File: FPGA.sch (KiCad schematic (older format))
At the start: 9 parts, among them U34 PCA9555AHF, U39 PCA9555AHF

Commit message: SCH: connect SI570_OE to U39 P0_0 (pin 1)
... also rotated 6 net labels to make the
little _not connected_ square disappear
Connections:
- net labels added: SI570_OE
- wire segments 147 -> 148
- no-connect marks 4 -> 3
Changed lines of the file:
@@
 I2C_APP_SDA
 NoConn ~ 8500 8950
-NoConn ~ 8500 9050
 NoConn ~ 8500 9850
 NoConn ~ 8500 9950
@@
 	1    0    0    -1
 $EndComp
+Text HLabel 8950 9050 2    50   Output ~ 10
+SI570_OE
+Wire Wire Line
+	8500 9050 8950 9050
 $EndSCHEMATC

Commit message: Start adding isolation for I2C_FPGA_SW_RST and EXP_INT
Adds U47, another TCA9517
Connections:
- net labels removed: +3V3
- wire segments 148 -> 149
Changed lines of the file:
@@
 Wire Wire Line
 	8550 3550 8700 3550
-$Comp
-L power:+3V3 #PWR?
-U 1 1 5DA3DD5C
-P 1100 8400
-AR Path="/5BD32060/5DA3DD5C" Ref="#PWR?"  Part="1"
-AR Path="/5C907554/5C417BCB/5DA3DD5C" Ref="#PWR?"  Part="1"
-AR Path="/5C907554/5DA3DD5C" Ref="#PWR0548"  Part="1"
-AR Path="/5C907554/5CAAC367/5DA3DD5C" Ref="#PWR?"  Part="1"
-F 0 "#PWR0548" H 1100 8250 50  0001 C CNN
-F 1 "+3V3" H 1115 8573 50  0000 C CNN
-F 2 "" H 1100 8400 50  0001 C CNN
-F 3 "" H 1100 8400 50  0001 C CNN
-	1    1100 8400
-	1    0    0    -1
-$EndComp
 Wire Wire Line
 	1100 9050 1100 8700
@@
 Wire Wire Line
 	8500 9050 8950 9050
+$Comp
+L power:+3V3P #PWR?
+U 1 1 5F5802EE
+P 1100 8350
+AR Path="/5C16C03C/5F5802EE" Ref="#PWR?"  Part="1"
+AR Path="/5BCEDA39/5F5802EE" Ref="#PWR?"  Part="1"
+AR Path="/5D05A99E/5F5802EE" Ref="#PWR?"  Part="1"
+AR Path="/5C16BF8E/5F5802EE" Ref="#PWR?"  Part="1"
+AR Path="/5CA40231/5F5802EE" Ref="#PWR?"  Part="1"
+AR Path="/5F5802EE" Ref="#PWR?"  Part="1"
+AR Path="/5BCEDA3D/5F5802EE" Ref="#PWR?"  Part="1"
+AR Path="/5C907554/5F5802EE" Ref="#PWR0548"  Part="1"
+F 0 "#PWR0548" H 1100 8200 50  0001 C CNN
+F 1 "+3V3P" H 1115 8523 50  0000 C CNN
+F 2 "" H 1100 8350 50  0001 C CNN
+F 3 "" H 1100 8350 50  0001 C CNN
+	1    1100 8350
+	1    0    0    -1
+$EndComp
+Wire Wire Line
+	1100 8400 1100 8350
 $EndSCHEMATC

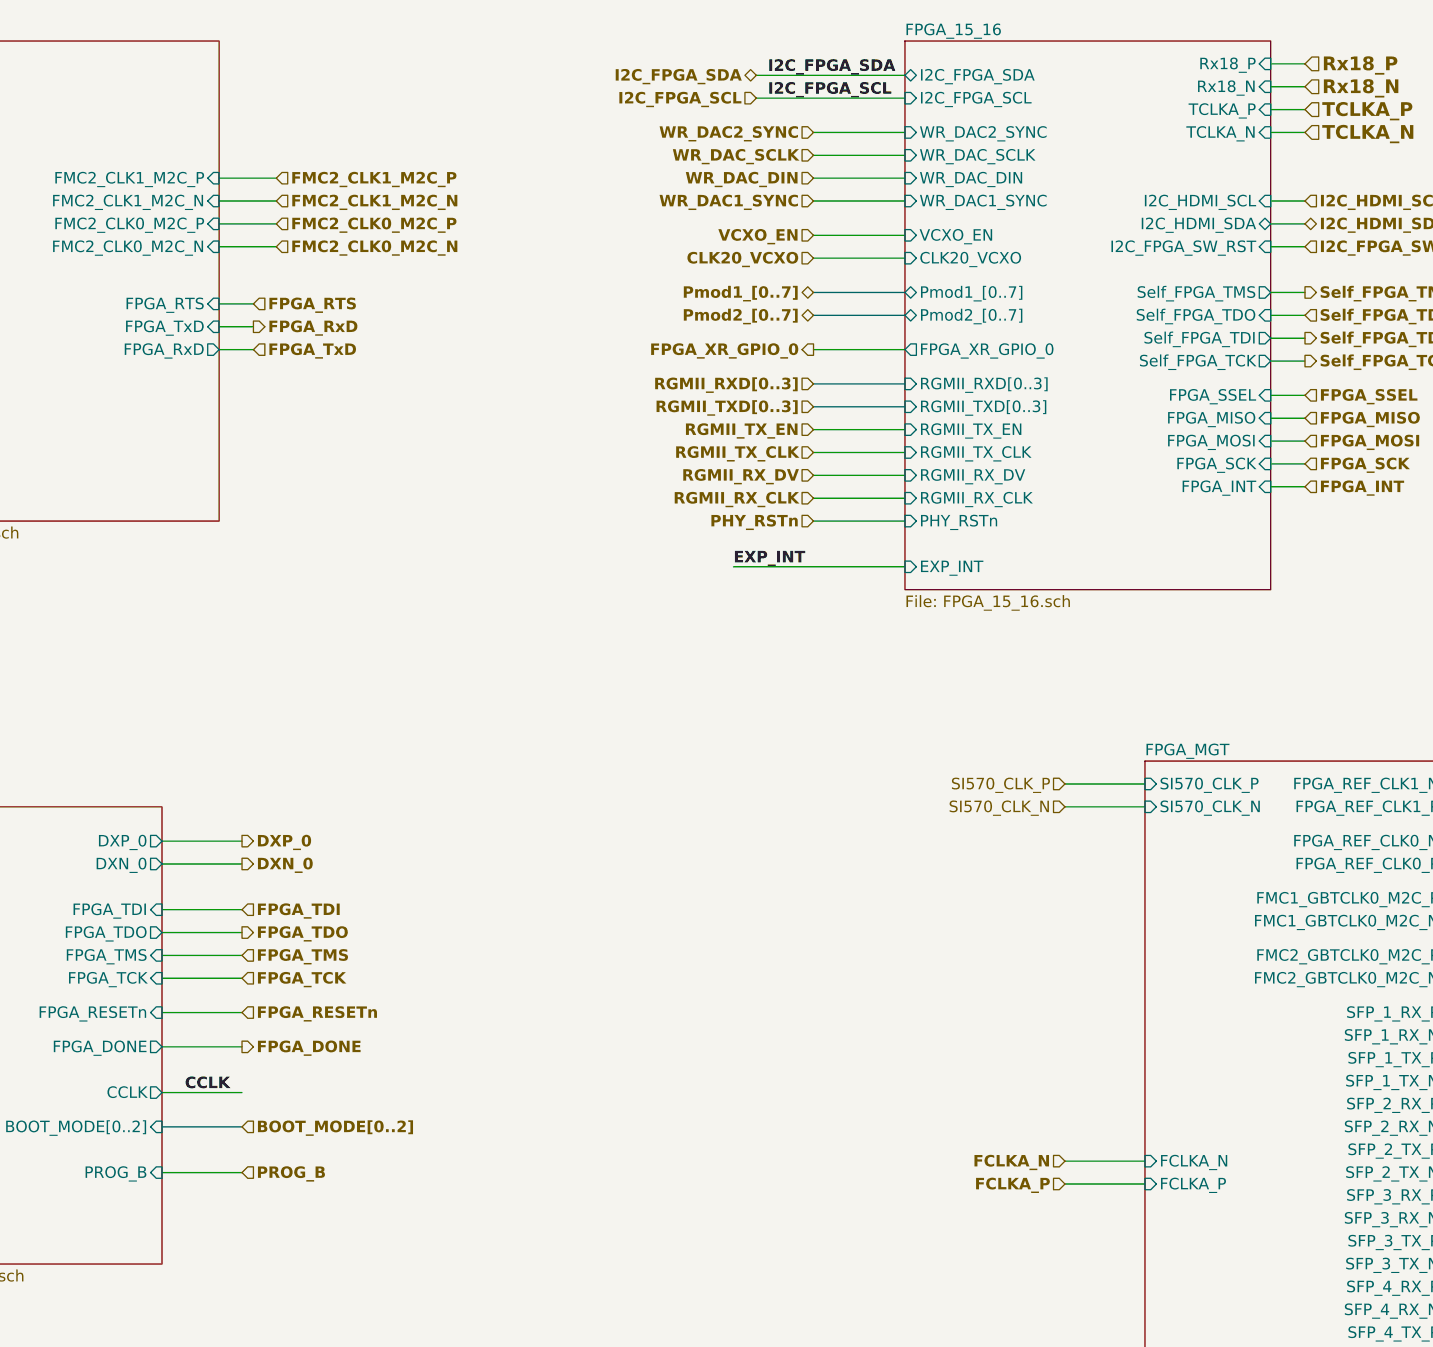
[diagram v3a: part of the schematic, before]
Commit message: sch: connect FPGA_DONE to U46, U47
also clean up some overlapping elements
and miss-aligned labels
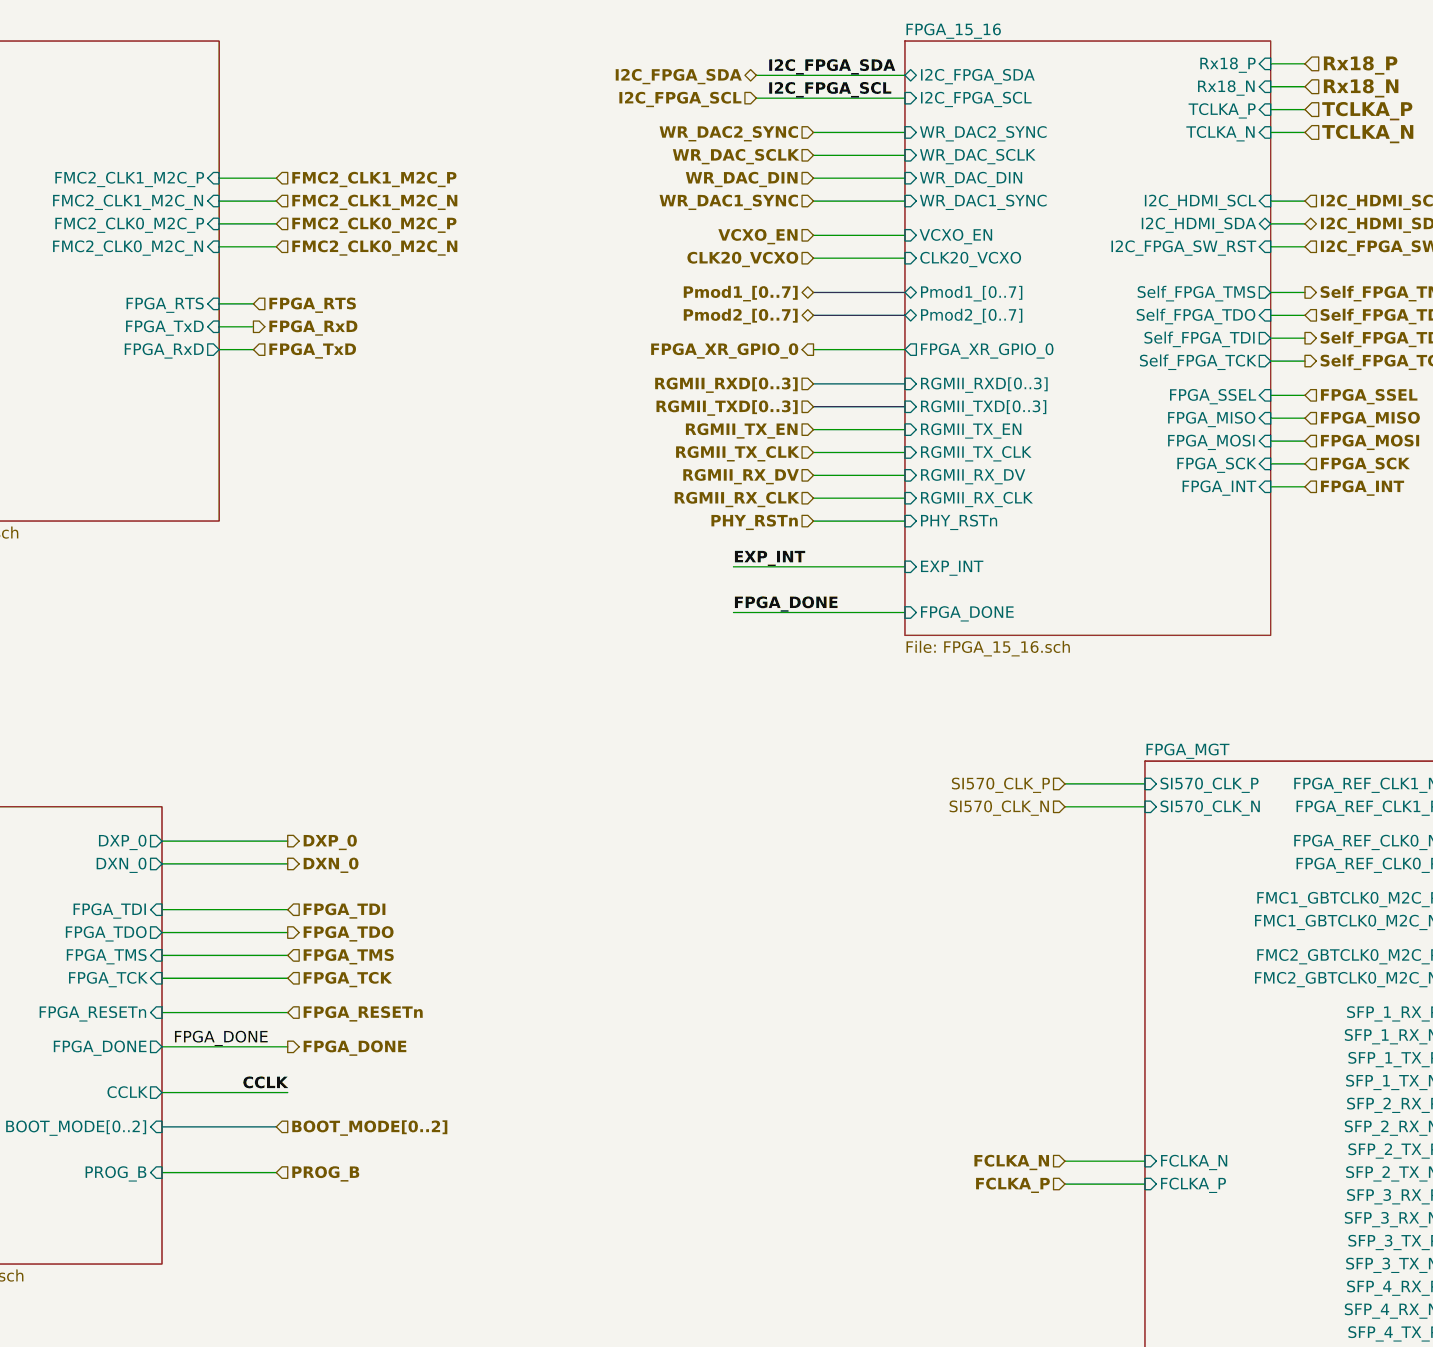
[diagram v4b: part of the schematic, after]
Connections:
- wire segments 149 -> 150
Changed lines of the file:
@@
 Comment4 ""
 $EndDescr
-Text HLabel 4050 5950 2    50   Input ~ 10
+Text HLabel 4250 5950 2    50   Input ~ 10
 FPGA_RESETn
 $Sheet
@@
 F12 "PROG_B" I R 3700 6650 50
 $EndSheet
-Wire Wire Line
-	3700 5950 4050 5950
-Text HLabel 4050 5500 2    50   Input ~ 10
+Text HLabel 4250 5500 2    50   Input ~ 10
 FPGA_TDI
-Text HLabel 4050 5600 2    50   Output ~ 10
+Text HLabel 4250 5600 2    50   Output ~ 10
 FPGA_TDO
-Text HLabel 4050 5700 2    50   Input ~ 10
+Text HLabel 4250 5700 2    50   Input ~ 10
 FPGA_TMS
-Text HLabel 4050 5800 2    50   Input ~ 10
+Text HLabel 4250 5800 2    50   Input ~ 10
 FPGA_TCK
-Wire Wire Line
-	4050 5500 3700 5500
-Wire Wire Line
-	4050 5600 3700 5600
-Wire Wire Line
-	4050 5700 3700 5700
-Wire Wire Line
-	4050 5800 3700 5800
-Text HLabel 4050 5200 2    50   Output ~ 10
+Text HLabel 4250 5200 2    50   Output ~ 10
 DXP_0
-Text HLabel 4050 5300 2    50   Output ~ 10
+Text HLabel 4250 5300 2    50   Output ~ 10
 DXN_0
-Wire Wire Line
-	3700 5200 4050 5200
-Wire Wire Line
-	4050 5300 3700 5300
-Text HLabel 4050 6100 2    50   Output ~ 10
-FPGA_DONE
-Wire Wire Line
-	4050 6100 3700 6100
 $Sheet
 S 8000 4850 1350 2800
@@
 Wire Wire Line
 	7650 6700 8000 6700
-Text HLabel 4050 6450 2    50   Input ~ 10
+Text HLabel 4200 6450 2    50   Input ~ 10
 BOOT_MODE[0..2]
 Wire Bus Line
-	3700 6450 4050 6450
+	3700 6450 4200 6450
 $Sheet
 S 2350 1700 1600 2100
@@
 $EndSheet
 $Sheet
-S 6950 1700 1600 2400
+S 6950 1700 1600 2600
 U 5CAAC367
 F0 "FPGA_15_16" 50
@@
 F35 "RGMII_RX_DV" I L 6950 3600 50
 F36 "RGMII_RX_CLK" I L 6950 3700 50
+F37 "FPGA_DONE" I L 6950 4200 50
 $EndSheet
 $Sheet
@@
 	8700 3650 8550 3650
 Wire Wire Line
-	4050 6300 3700 6300
-Text Label 3800 6300 0    50   ~ 10
+	4250 6300 3700 6300
+Text Label 4250 6300 2    50   ~ 10
 CCLK
 Text Label 9550 2100 0    50   ~ 10
@@
 Wire Wire Line
 	8550 2500 8700 2500
-Text HLabel 4050 6650 2    50   Input ~ 10
+Text HLabel 4200 6650 2    50   Input ~ 10
 PROG_B
 Wire Wire Line
-	4050 6650 3700 6650
+	4200 6650 3700 6650
 $Comp
 L power:GND #PWR?
@@
 Wire Wire Line
 	1100 8400 1100 8350
+Wire Wire Line
+	4250 6100 3700 6100
+Text HLabel 4250 6100 2    50   Output ~ 10
+FPGA_DONE
+Text Label 3750 6100 0    50   ~ 0
+FPGA_DONE
+Wire Wire Line
+	6950 4200 6200 4200
+Text Label 6200 4200 0    50   ~ 10
+FPGA_DONE
+Wire Wire Line
+	3700 5200 4250 5200
+Wire Wire Line
+	3700 5300 4250 5300
+Wire Wire Line
+	3700 5500 4250 5500
+Wire Wire Line
+	3700 5600 4250 5600
+Wire Wire Line
+	3700 5700 4250 5700
+Wire Wire Line
+	3700 5800 4250 5800
+Wire Wire Line
+	3700 5950 4250 5950
 $EndSCHEMATC
